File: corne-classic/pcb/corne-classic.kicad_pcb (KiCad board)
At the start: 2 copper layers, 133.8 x 92.2 mm, 98 parts, among them J3 LED, P1 i2c-pin, P2 i2c-pin, SW1 SW_PUSH, SW10 SW_PUSH, SW11 SW_PUSH, SW12 SW_PUSH, SW13 SW_PUSH, SW14 SW_PUSH, SW15 SW_PUSH, SW16 SW_PUSH, SW17 SW_PUSH, SW18 SW_PUSH, SW19 SW_PUSH, SW2 SW_PUSH, SW20 SW_PUSH, SW21 SW_PUSH, SW3 SW_PUSH, SW4 SW_PUSH, SW5 SW_PUSH, SW6 SW_PUSH, SW7 SW_PUSH, SW8 SW_PUSH, SW9 SW_PUSH, U1 ProMicro

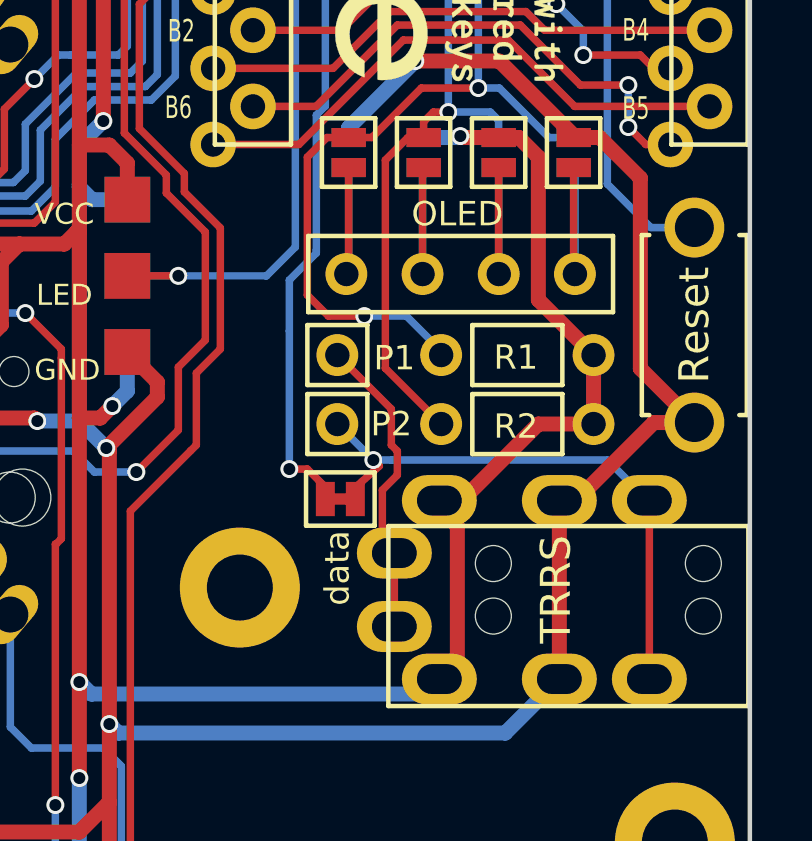
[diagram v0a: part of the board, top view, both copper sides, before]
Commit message: Update refs in pcbnew
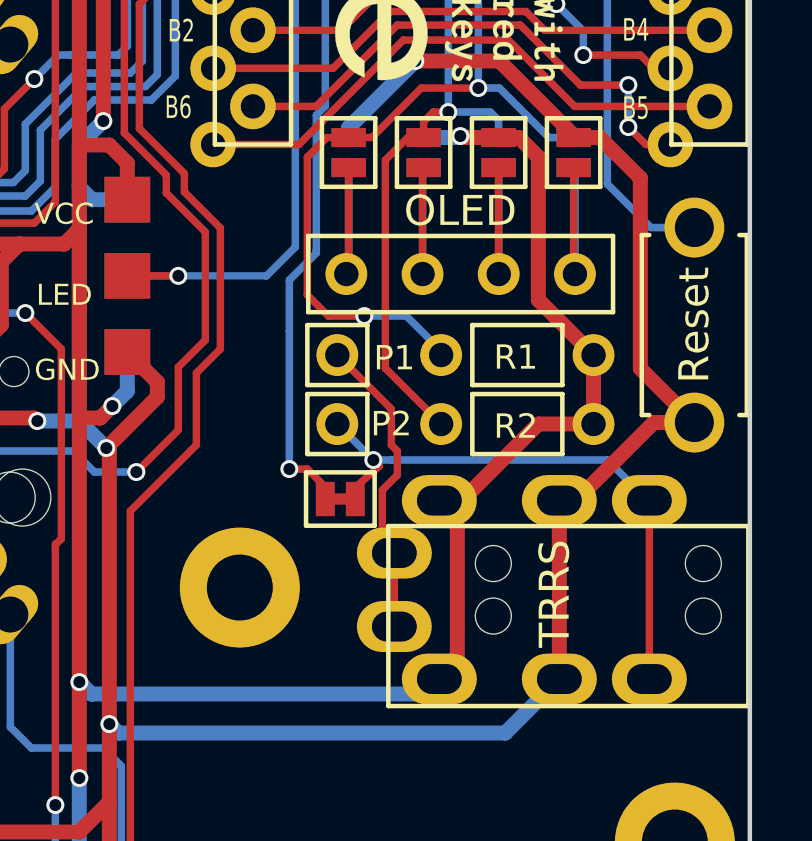
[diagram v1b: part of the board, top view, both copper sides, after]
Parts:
- renumbered TRRS to J1, OLED to J2, data to JP1, L22 to L1, L4 to L10, L5 to L11, L6 to L12, L7 to L13, L8 to L14, L9 to L15, L10 to L16, L11 to L17, L12 to L18, L13 to L19, L23 to L2, L14 to L20, L15 to L21, L16 to L22, L17 to L23, L18 to L24, L19 to L25, L20 to L26, L21 to L27, L24 to L3, L25 to L4, L26 to L5, L27 to L6, L1 to L7, L2 to L8, L3 to L9

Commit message: fixed typo
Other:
- board text added: "Corne Classic v2.0 PCB designed by foostan"
- board text removed: "Corne Classic v2.0 PCB Designed by foostan"
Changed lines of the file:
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@@
   )
   (target plus (at 194.8 63.4) (size 5) (width 0.15) (layer Edge.Cuts))
-  (gr_text "Corne Classic v2.0\nPCB Designed by foostan" (at 119.4 121.5) (layer B.Mask)
+  (gr_text "Corne Classic v2.0\nPCB designed by foostan" (at 119.4 121.5) (layer B.Mask)
     (effects (font (size 1 1) (thickness 0.125)) (justify left mirror))
   )
-  (gr_text "Corne Classic v2.0\nPCB Designed by foostan" (at 100.1 121.5) (layer F.Mask)
+  (gr_text "Corne Classic v2.0\nPCB designed by foostan" (at 100.1 121.5) (layer F.Mask)
     (effects (font (size 1 1) (thickness 0.125)) (justify left))
   )

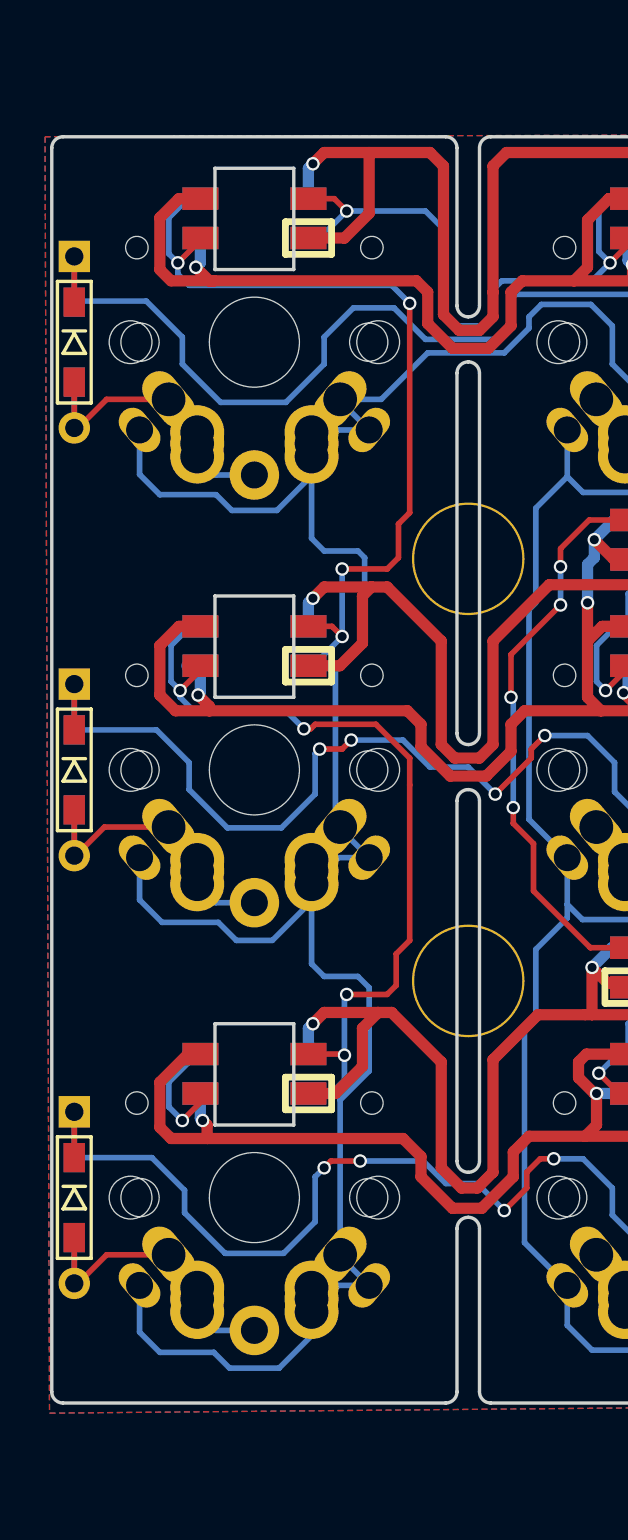
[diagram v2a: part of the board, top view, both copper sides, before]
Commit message: removed break off cuts
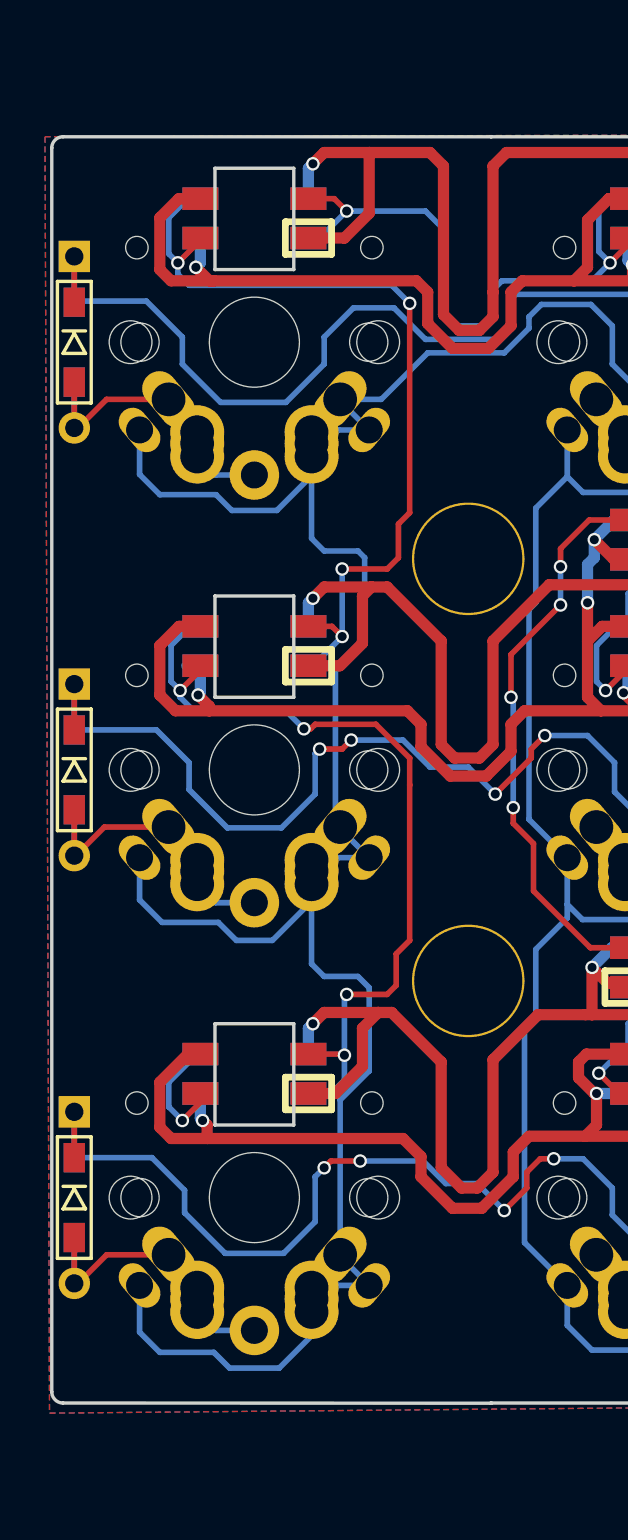
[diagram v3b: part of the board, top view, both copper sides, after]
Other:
- outline, holes or cut-outs redrawn
- rule pad_to_mask_clearance: 0.2 -> 0

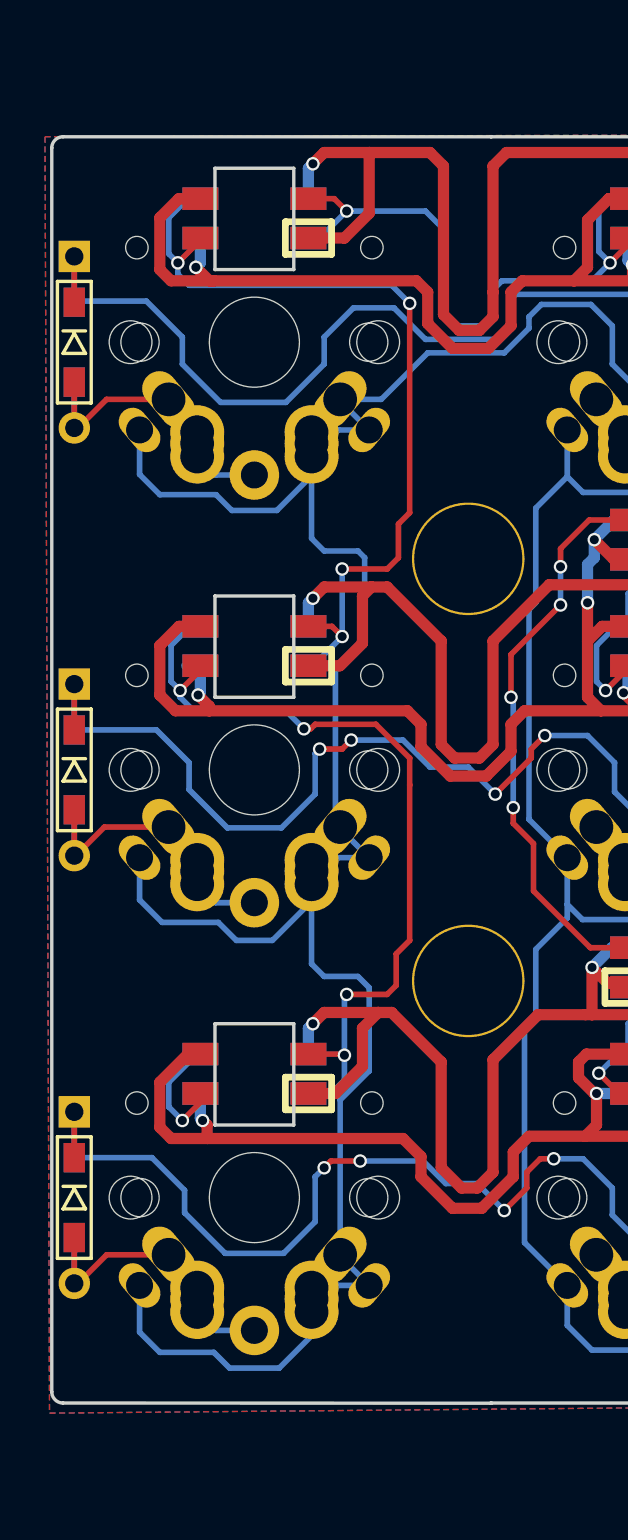
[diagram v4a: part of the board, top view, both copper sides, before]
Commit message: reverted corne classic to original, made new folder
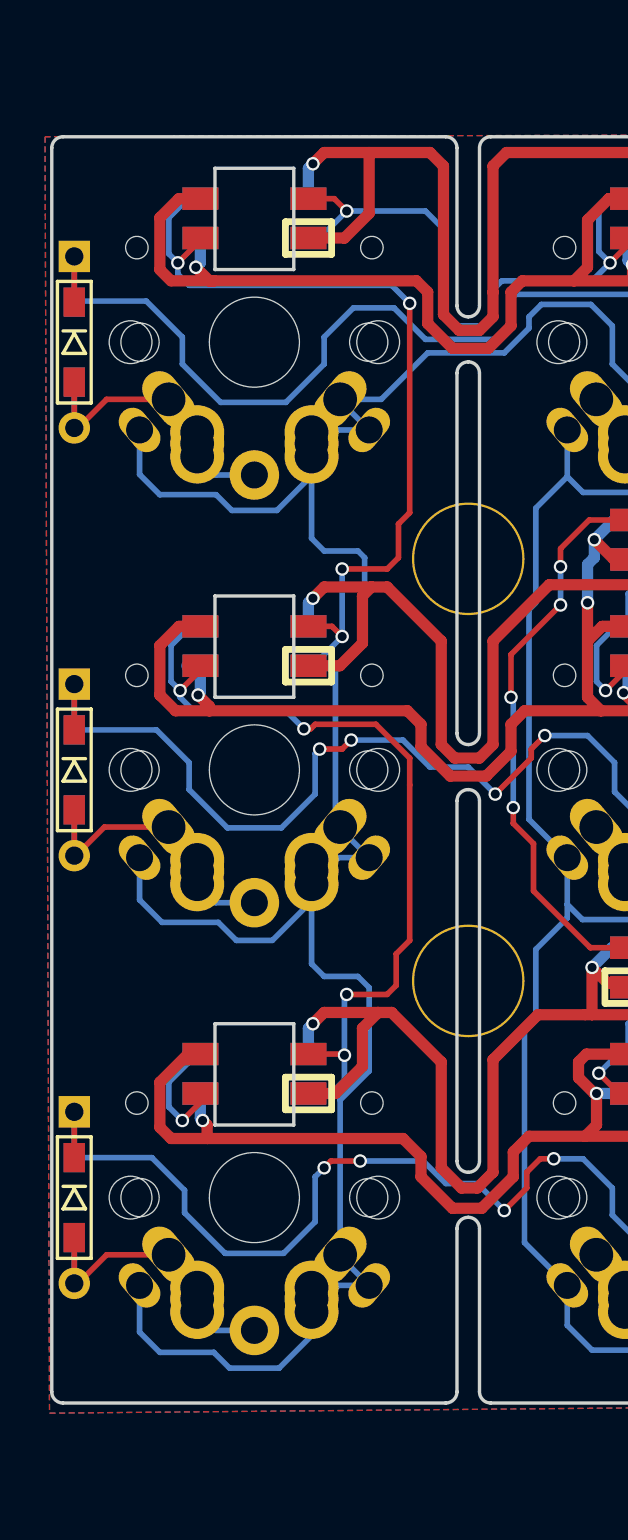
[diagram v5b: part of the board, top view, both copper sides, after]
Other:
- outline, holes or cut-outs redrawn
- rule pad_to_mask_clearance: 0 -> 0.2
